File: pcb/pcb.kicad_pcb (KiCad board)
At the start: 2 copper layers, 28 parts, among them J1 Conn_01x02, J2 Conn_01x02, SW1 SW_SPDT, U1 TL072, U3 AP63205WU

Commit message: pcb v1
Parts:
- added H1: MountingHole_Pad, MountingHole:MountingHole_2.2mm_M2, F.Cu at (120.5, 46.6)
- added H2: MountingHole_Pad, MountingHole:MountingHole_2.2mm_M2, F.Cu at (120.5, 26.1)
- added H3: MountingHole_Pad, MountingHole:MountingHole_2.2mm_M2, F.Cu at (86.2, 26.1)
- added H4: MountingHole_Pad, MountingHole:MountingHole_2.2mm_M2, F.Cu at (86.2, 46.6)
- C1, C3, C4, C5, C6, R1, R2, R3, R4, R7, R8, SW1: moved to B.Cu
- moved J1 64.8 mm to (102.0, 26.5), turned to 90 degrees
- moved SW1 47.1 mm to (112.2, 25.9)
- moved J2 43.4 mm to (85.8, 32.7), turned to 90 degrees
- moved C4 34.6 mm to (96.0, 42.9), turned to 90 degrees
- moved C2 33.3 mm to (93.0, 34.2)
- moved R8 31.0 mm to (99.1, 40.3), turned to 90 degrees
- moved R7 30.8 mm to (99.1, 42.1), turned to 90 degrees
- moved R5 30.2 mm to (94.5, 35.5), turned to -90 degrees
- moved R4 26.8 mm to (91.8, 37.5), turned to 180 degrees
- moved C6 25.9 mm to (90.4, 41.4), turned to 180 degrees
- moved C5 25.7 mm to (90.4, 40.4)
- moved R3 24.2 mm to (89.5, 37.5), turned to 180 degrees
- moved C1 23.8 mm to (85.2, 38.6), turned to 180 degrees
- moved C3 23.6 mm to (95.0, 42.9), turned to -90 degrees
- moved R2 23.1 mm to (85.2, 39.6), turned to 180 degrees
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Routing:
- net GNDPWR: track 8.32 -> 73.6 mm, vias 0 -> 4
- net GND: track 2.34 -> 52.4 mm
- net +9V: track 2.41 -> 43.1 mm
- net Net-(J1-Pin_1): track 0.00 -> 12.3 mm
- net Net-(U1A-+): track 0.00 -> 5.69 mm
- net Net-(U1A--): track 0.00 -> 3.91 mm
- net Net-(C2-Pad1): track 0.00 -> 3.30 mm
- net Net-(C1-Pad2): track 0.00 -> 2.00 mm
- net Net-(C2-Pad2): track 0.00 -> 1.86 mm
- added copper zone on B.Cu, net GNDPWR
- added copper zone on F.Cu, net GNDPWR
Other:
- board outline added: 41.2 x 25.6 mm

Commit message: pcb v2
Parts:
- removed C11: 22u, Capacitor_SMD:C_0402_1005Metric
- removed C12: 10u, Capacitor_SMD:C_0402_1005Metric
- removed L1: 4u7, Resistor_SMD:R_0402_1005Metric
- added C13: 1u, Capacitor_SMD:C_0402_1005Metric, F.Cu at (90.7, 64.1)
- added R10: 4k7, Resistor_SMD:R_0402_1005Metric, F.Cu at (92.7, 64.0)
- added R11: 10k, Resistor_SMD:R_0402_1005Metric, F.Cu at (91.3, 66.0)
- added R9: 100k, Resistor_SMD:R_0402_1005Metric, F.Cu at (90.7, 65.0)
- added RV2: 100k, Connector_PinHeader_2.54mm:PinHeader_1x03_P2.54mm_Vertical, F.Cu at (85.7, 69.1)
- C1, C3, C4, C5, C6, R2, R4, R7, R8, SW1: moved to F.Cu
- C10: value 22u -> 0.1u
- C9: value 100n -> 0.22u
- R1: value 1M -> 1k; moved to F.Cu
- R3: value 10k -> 5k; moved to F.Cu
- R6: value 47 -> 10k
- RV1: value R_Potentiometer -> 100k
- U1: moved to B.Cu
- U3: value AP63205WU -> LM7805_TO220; footprint Package_TO_SOT_SMD:TSOT-23-6 -> LM7805MP_NOPB:VREG_LM7805MP_NOPB
- moved J1 49.7 mm to (115.8, 74.3)
- moved SW1 49.5 mm to (109.5, 75.4)
- moved H2 49.1 mm to (123.2, 75.1)
- moved H3 49.0 mm to (85.1, 75.1)
- moved J2 42.6 mm to (97.5, 73.7)
- moved C2 35.4 mm to (90.6, 69.6), turned to 180 degrees
- moved R5 35.2 mm to (90.6, 70.5), turned to 0 degrees
- moved R6 34.4 mm to (90.2, 67.8)
- moved R8 34.0 mm to (103.1, 74.0), turned to 0 degrees
- moved C8 32.6 mm to (101.3, 65.0)
- moved C1 32.6 mm to (94.1, 70.0)
- moved C5 32.4 mm to (100.7, 71.0)
- moved R7 31.2 mm to (103.1, 73.0), turned to 180 degrees
- moved C6 30.5 mm to (100.7, 70.1)
- moved R3 30.0 mm to (94.1, 67.1)
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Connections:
- C1 pad 1: GND -> Net-(J2-Pin_1)
- C2 pad 2: Net-(C2-Pad2) -> Net-(U1B-+)
- C9 pad 1: Net-(U3-SW) -> +9V
- C9 pad 2: Net-(U3-BST) -> GNDPWR
- J2 pad 1: GND -> Net-(J2-Pin_1)
- R5 pad 1: Net-(C2-Pad2) -> Net-(U1B-+)
- R6 pad 1: Net-(C2-Pad2) -> GND
- R6 pad 2: GND -> Net-(U1B--)
- RV1 pad 1: GND -> GNDPWR
- RV1 pad 3: GND -> Net-(R10-Pad1)
- U1 pad 5: unconnected-(U1B-+-Pad5) -> Net-(U1B-+)
- U1 pad 6: unconnected-(U1B---Pad6) -> Net-(U1B--)
- U1 pad 7: unconnected-(U1-Pad7) -> Net-(C13-Pad1)
- U3 pad 1: +5V -> +9V
- U3 pad 2: +9V -> GNDPWR
- U3 pad 3: +9V -> +5V
- U3 pad 4: GNDPWR -> (no net)
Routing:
- net GNDPWR: track 73.6 -> 23.4 mm, vias 4 -> 0
- net +9V: track 43.1 -> 73.4 mm, vias 0 -> 2
- net Net-(R10-Pad1): track 0.00 -> 9.39 mm, vias 0 -> 1
- net Net-(C2-Pad1): track 3.30 -> 9.91 mm
- net Net-(J1-Pin_1): track 12.3 -> 6.58 mm
- net Net-(C13-Pad1): track 0.00 -> 5.55 mm
- net Net-(U1B--): track 0.00 -> 5.25 mm
- net Net-(J2-Pin_1): track 0.00 -> 4.89 mm
- net Net-(U1A-+): track 5.69 -> 2.01 mm
- net Net-(U2-AUDIO_L): track 10.5 -> 7.08 mm
- net GND: track 52.4 -> 55.8 mm
- net Net-(U1B-+): track 0.00 -> 2.80 mm
- net Net-(C13-Pad2): track 0.00 -> 2.58 mm
- net Net-(U3-SW): track 2.39 -> 0.00 mm
- net Net-(C2-Pad2): track 1.86 -> 0.00 mm
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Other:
- board size 41.2 x 25.6 mm -> 43.4 x 25.6 mm

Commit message: change caps, do bom, reroute, readme, ship, etc
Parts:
- C10: value 0.1u -> 100n
- C4, C6: footprint Capacitor_SMD:C_0402_1005Metric -> Capacitor_SMD:C_0805_2012Metric
- C7: footprint Capacitor_SMD:C_0402_1005Metric -> Capacitor_SMD:C_1206_3216Metric
- R3: value 5k -> 4k7
- U2: value ~ -> BT
- moved C10 2.03 mm to (89.6, 57.6)
- moved C9 2.03 mm to (89.6, 55.0)
- moved U3 2.03 mm to (94.3, 56.5)
- moved J2 1.69 mm to (96.1, 74.6)
- moved C5 1.25 mm to (100.7, 72.3)
- moved C7 0.97 mm to (100.8, 58.5)
- moved C4 0.95 mm to (91.4, 61.6)
- moved R7 0.75 mm to (103.1, 73.8)
- moved R8 0.75 mm to (103.1, 74.8)
- moved C6 0.72 mm to (100.2, 70.6)
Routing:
- net +9V: track 73.4 -> 77.6 mm
- net +5V: track 11.6 -> 15.1 mm
- net GND: track 55.8 -> 59.0 mm
- net GNDPWR: track 23.4 -> 25.0 mm

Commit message: logo & silkscreen art
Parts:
- added G***: LOGO, LOGO, F.Cu at (113.9, 63.3)
- added G***: LOGO, LOGO, B.Cu at (111.3, 64.2)
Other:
- board text added: "made w/ love by @wenbang24"

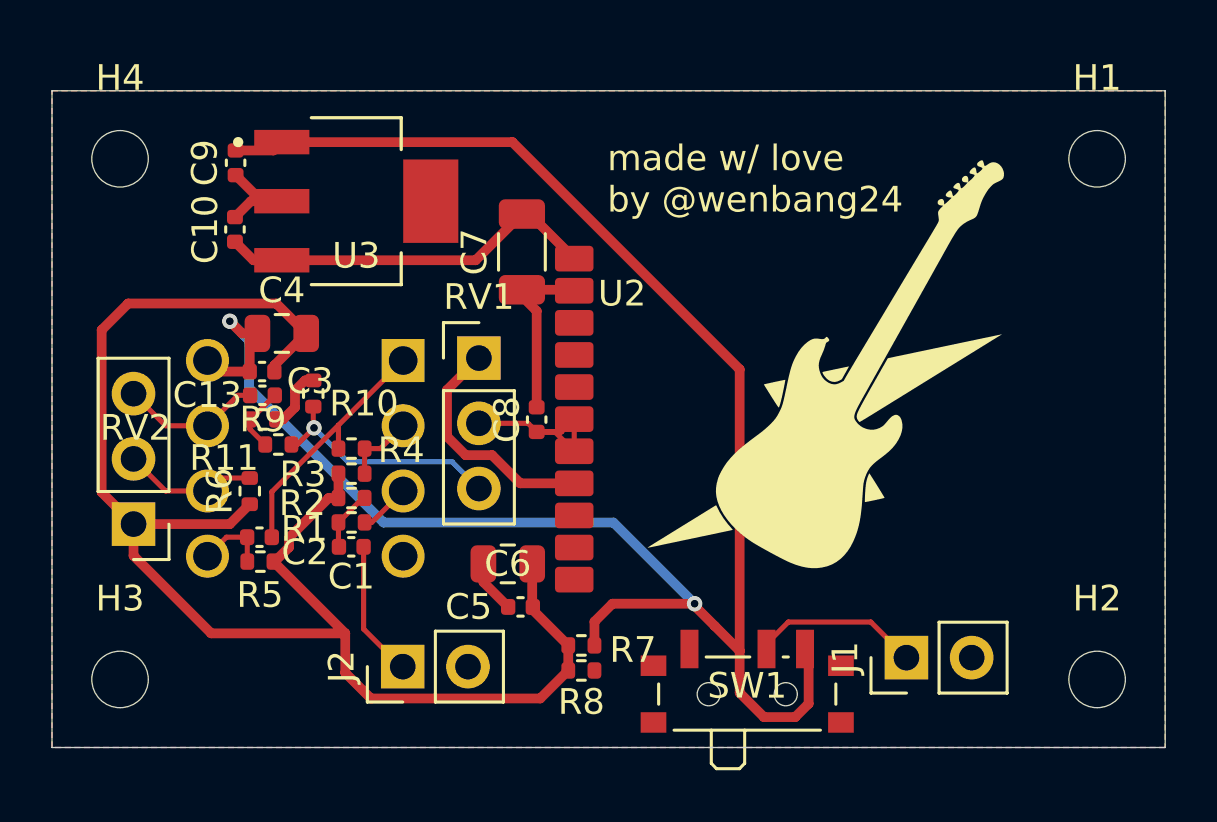
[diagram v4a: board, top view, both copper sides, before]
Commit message: connect button footprint
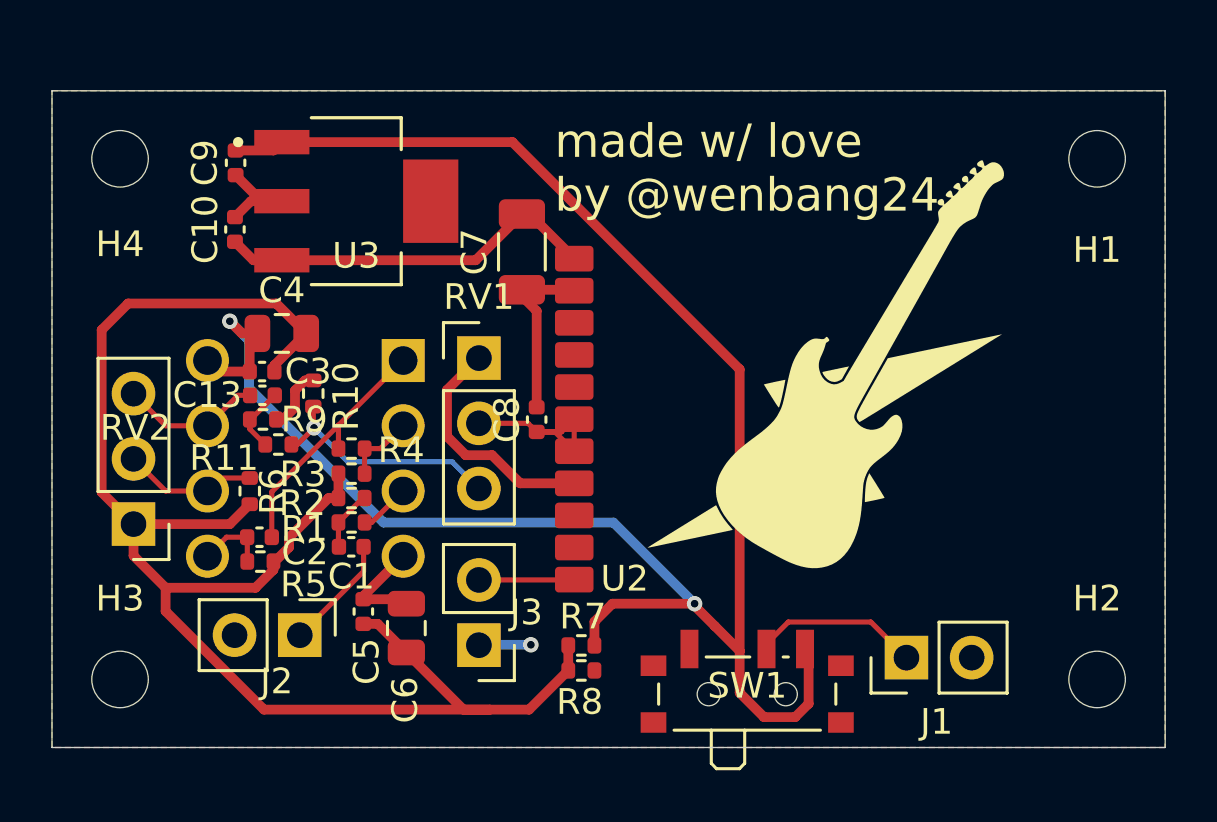
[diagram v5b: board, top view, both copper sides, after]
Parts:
- added J3: Conn_01x02, Connector_PinHeader_2.54mm:PinHeader_1x02_P2.54mm_Vertical, F.Cu at (99.1, 73.8)
- moved C5 6.12 mm to (94.6, 72.5), turned to -90 degrees
- moved C6 4.67 mm to (96.3, 73.1), turned to 90 degrees
- moved J2 4.19 mm to (92.1, 73.4), turned to -90 degrees
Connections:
- U2 pad 11: unconnected-(U2-CONNECT-Pad11) -> Net-(J3-Pin_2)
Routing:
- net GNDPWR: track 25.0 -> 29.0 mm, vias 0 -> 1
- net Net-(J3-Pin_2): track 0.00 -> 3.72 mm
- net GND: track 59.0 -> 62.4 mm
- net Net-(J2-Pin_1): track 5.33 -> 4.47 mm
